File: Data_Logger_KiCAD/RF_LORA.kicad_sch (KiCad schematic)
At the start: 14 parts, among them U6 SX1262IMLTRT, U7 MASW-007221, Y1 Crystal_GND24

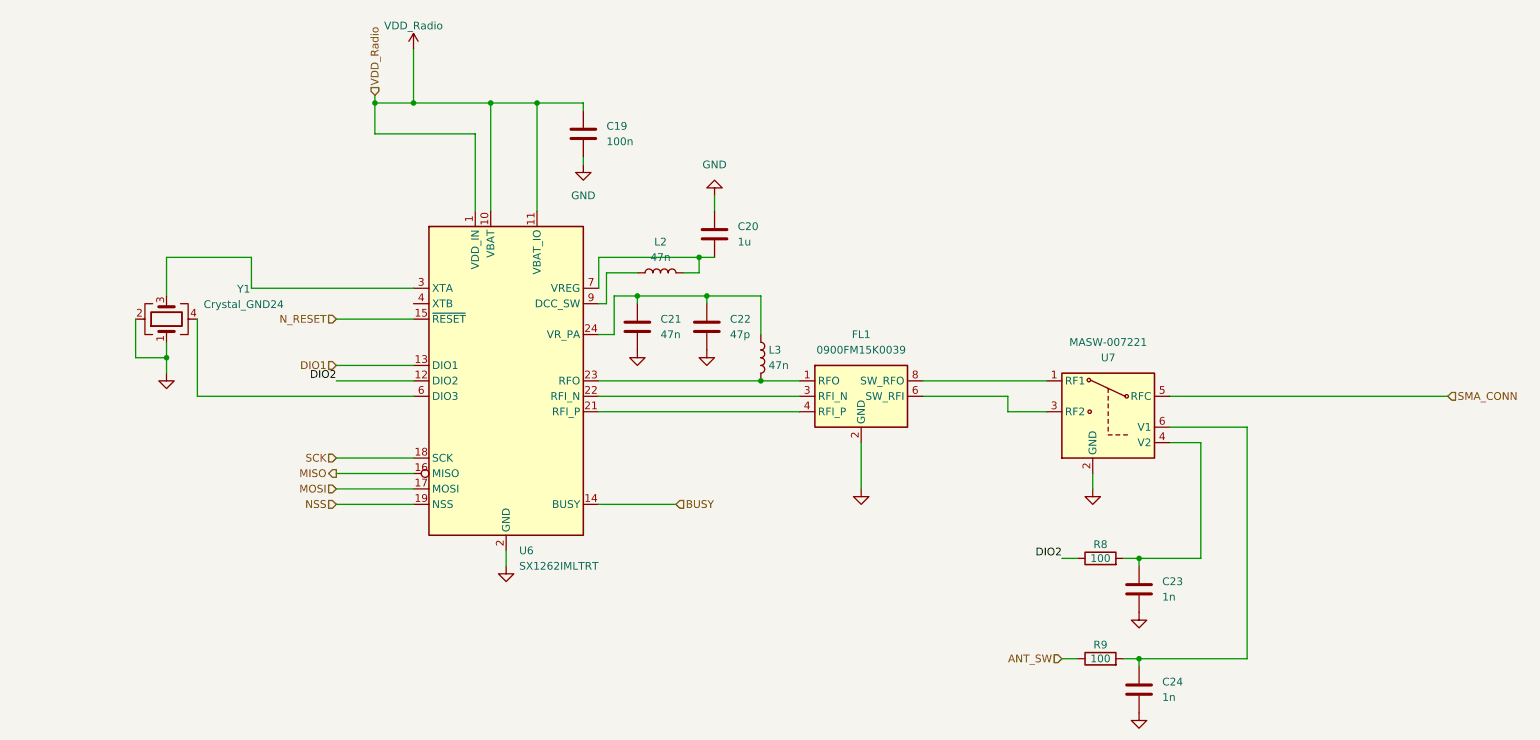
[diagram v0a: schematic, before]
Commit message: Added NT2016 TCXO Symbol and Footprint
Added NT2016 TCXO Symbol and Footprint
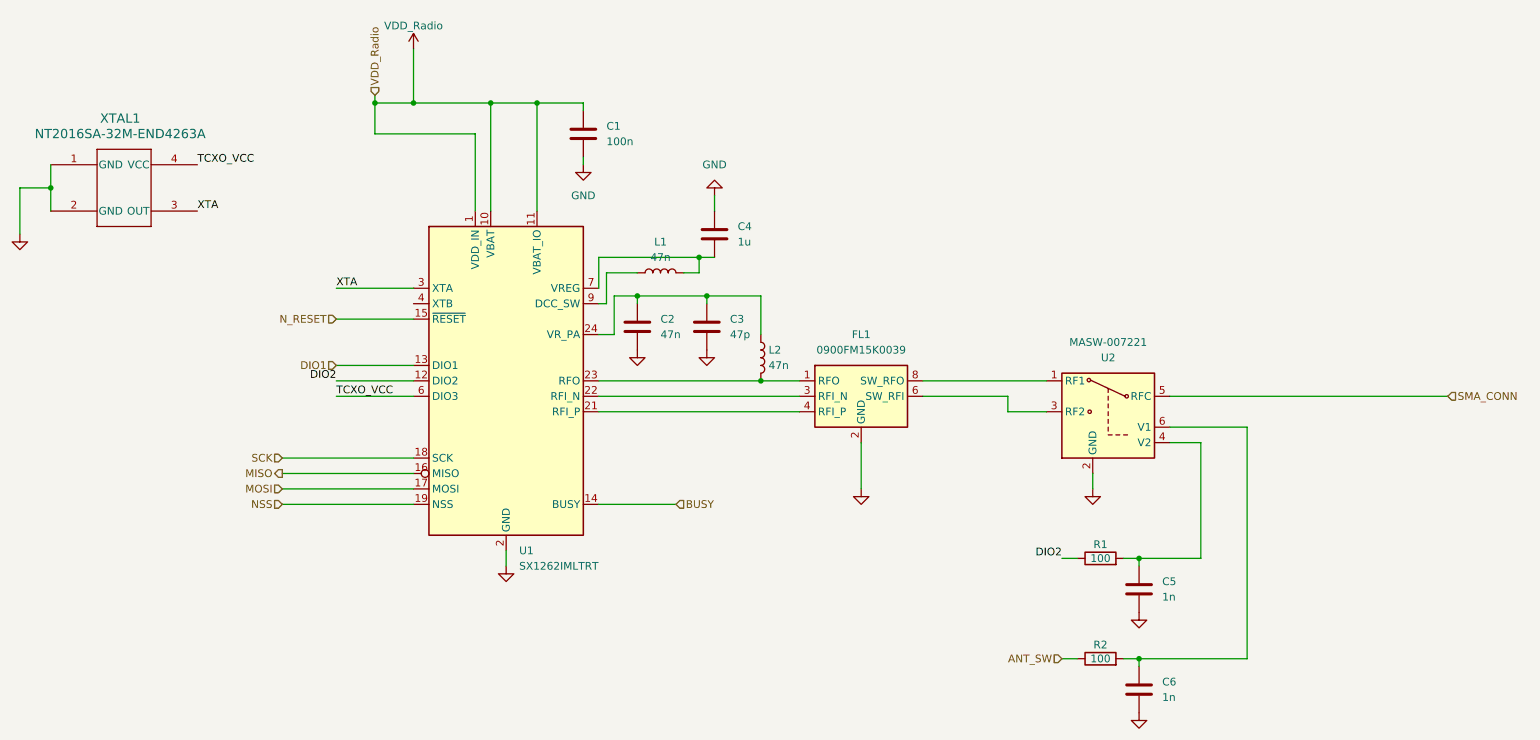
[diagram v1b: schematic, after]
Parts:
- removed Y1: Crystal_GND24, Crystal:Crystal_SMD_2520-4Pin_2.5x2.0mm, symbol Device:Crystal_GND24
- added XTAL1: NT2016SA-32M-END4263A, NT2016Footprints:NT2016SA-32M-END4263A_NDK, symbol NT2016_TCXO:NT2016SA-32M-END4263A
- renumbered C19 to C1, C21 to C2, C22 to C3, C20 to C4, C23 to C5, C24 to C6, L2 to L1, L3 to L2, R8 to R1, R9 to R2, U6 to U1, U7 to U2
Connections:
- net GND: now also XTAL1.1 (GND), XTAL1.2 (GND)
- net XTA: now reaches U1.3 (XTA)
- net XTA: now also XTAL1.3 (OUT)
- net TCXO_VCC: now reaches U1.6 (DIO3)
- net TCXO_VCC: now also XTAL1.4 (VCC)

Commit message: Magnetometer Footprint Added
Magnetometer Footprint Added
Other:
- company: (none) -> OSU ASDT
- title: (none) -> ASDT RF LoRa Schematic
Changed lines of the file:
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@@
 	(generator_version "9.0")
 	(paper "A4")
+	(title_block
+		(title "ASDT RF LoRa Schematic")
+		(rev "1.2 Last Rev:11/22/2025")
+		(company "OSU ASDT")
+		(comment 1 "Author: John Fletcher")
+	)
 	(junction
 		(at 96.52 38.1)

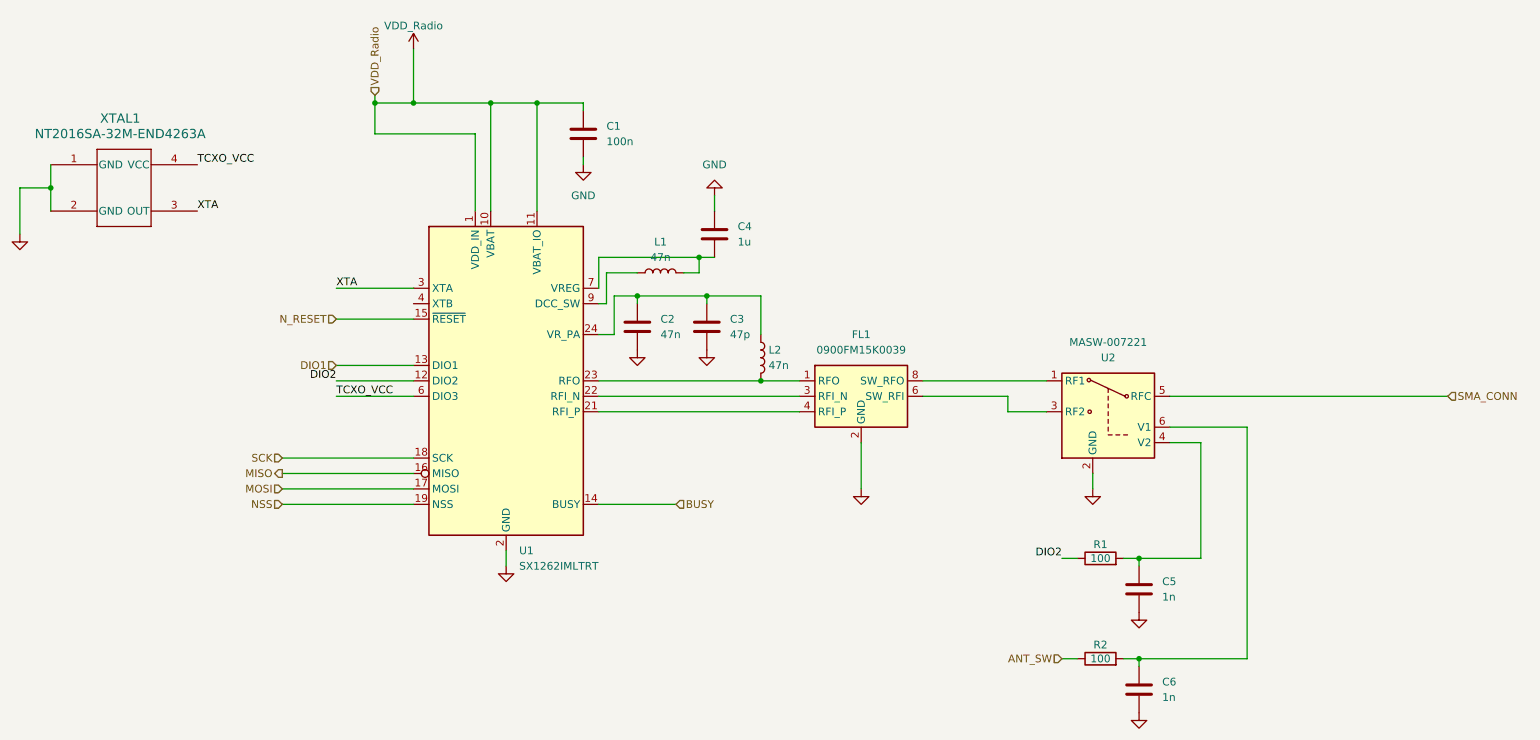
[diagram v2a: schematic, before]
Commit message: synced sheet pins in Data_Logger_Board_pro
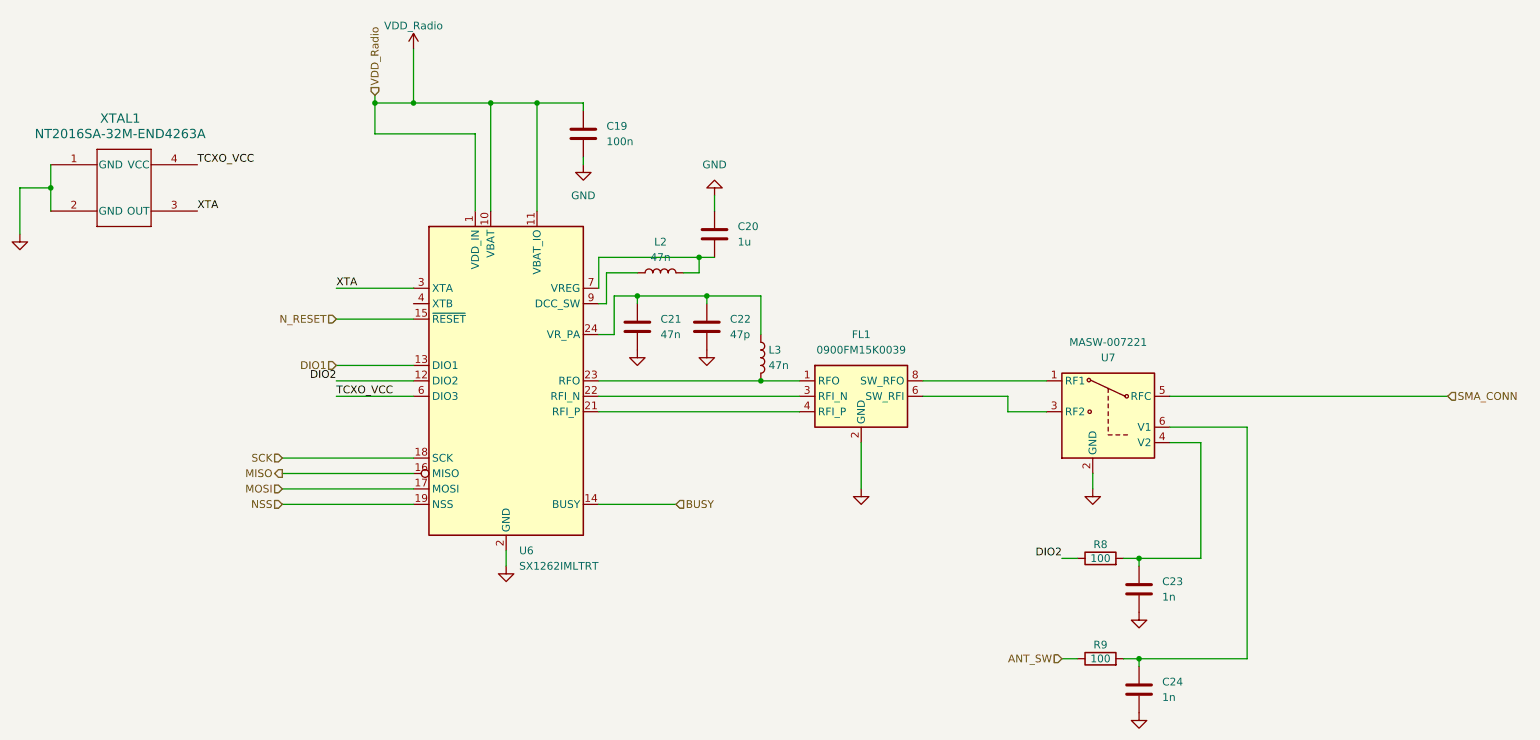
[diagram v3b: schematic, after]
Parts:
- renumbered C1 to C19, C4 to C20, C2 to C21, C3 to C22, C5 to C23, C6 to C24, L1 to L2, L2 to L3, R1 to R8, R2 to R9, U1 to U6, U2 to U7
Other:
- company: OSU ASDT -> (none)
- title: ASDT RF LoRa Schematic -> (none)
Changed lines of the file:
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@@
 	(generator_version "9.0")
 	(paper "A4")
-	(title_block
-		(title "ASDT RF LoRa Schematic")
-		(rev "1.2 Last Rev:11/22/2025")
-		(company "OSU ASDT")
-		(comment 1 "Author: John Fletcher")
-	)
 	(junction
 		(at 96.52 38.1)
@@
 		(dnp no)
 		(fields_autoplaced yes)
-		(property "Reference" "#PWR0105"
+		(property "Reference" "#PWR041"
 			(at 195.58 107.95 0)
 			(effects
@@
 		(on_board yes)
 		(dnp no)
-		(property "Reference" "R2"
+		(property "Reference" "R9"
 			(at 196.85 127.254 90)
 			(effects
@@
 		(dnp no)
 		(fields_autoplaced yes)
-		(property "Reference" "#PWR0108"
+		(property "Reference" "#PWR035"
 			(at 111.76 54.61 0)
 			(effects
@@
 		(on_board yes)
 		(dnp no)
-		(property "Reference" "U2"
+		(property "Reference" "U7"
 			(at 198.12 80.01 0)
 			(effects
@@
 		(dnp no)
 		(fields_autoplaced yes)
-		(property "Reference" "#PWR0103"
+		(property "Reference" "#PWR044"
 			(at 203.2 144.78 0)
 			(effects
@@
 		(dnp no)
 		(fields_autoplaced yes)
-		(property "Reference" "#PWR0101"
+		(property "Reference" "#PWR034"
 			(at 83.82 33.02 0)
 			(effects
@@
 		(dnp no)
 		(fields_autoplaced yes)
-		(property "Reference" "#PWR0106"
+		(property "Reference" "#PWR042"
 			(at 99.06 120.65 0)
 			(effects
@@
 		(dnp no)
 		(fields_autoplaced yes)
-		(property "Reference" "U1"
+		(property "Reference" "U6"
 			(at 101.2033 111.76 0)
 			(effects
@@
 		(dnp no)
 		(fields_autoplaced yes)
-		(property "Reference" "L1"
+		(property "Reference" "L2"
 			(at 124.46 60.96 90)
 			(effects
@@
 		(dnp no)
 		(fields_autoplaced yes)
-		(property "Reference" "L2"
+		(property "Reference" "L3"
 			(at 142.24 78.7399 0)
 			(effects
@@
 		(dnp no)
 		(fields_autoplaced yes)
-		(property "Reference" "#PWR0109"
+		(property "Reference" "#PWR036"
 			(at 133.35 46.99 0)
 			(effects
@@
 		(dnp no)
 		(fields_autoplaced yes)
-		(property "Reference" "C5"
+		(property "Reference" "C23"
 			(at 207.01 116.8399 0)
 			(effects
@@
 		(dnp no)
 		(fields_autoplaced yes)
-		(property "Reference" "#PWR0102"
+		(property "Reference" "#PWR040"
 			(at 157.48 107.95 0)
 			(effects
@@
 		(dnp no)
 		(fields_autoplaced yes)
-		(property "Reference" "#PWR0104"
+		(property "Reference" "#PWR043"
 			(at 203.2 128.27 0)
 			(effects
@@
 		(on_board yes)
 		(dnp no)
-		(property "Reference" "R1"
+		(property "Reference" "R8"
 			(at 196.85 110.744 90)
 			(effects
@@
 		(on_board yes)
 		(dnp no)
-		(property "Reference" "#PWR0110"
+		(property "Reference" "#PWR038"
 			(at 132.08 85.09 0)
 			(effects
@@
 		(on_board yes)
 		(dnp no)
-		(property "Reference" "C2"
+		(property "Reference" "C21"
 			(at 124.46 73.6599 0)
 			(effects
@@
 		(dnp no)
 		(fields_autoplaced yes)
-		(property "Reference" "C3"
+		(property "Reference" "C22"
 			(at 135.89 73.6599 0)
 			(effects
@@
 		(dnp no)
 		(fields_autoplaced yes)
-		(property "Reference" "XTAL1"
+		(property "Reference" "XTAL?"
 			(at 35.56 40.64 0)
 			(effects
@@
 				(path "/8ae4759a-151c-407c-bd9a-b8440b531f27"
 					(reference "XTAL1")
+					(unit 1)
+				)
+			)
+			(project "Data_Logger_Board"
+				(path "/db968e42-3ace-4cc9-9096-9d8f48135c40/795ab2be-9db7-4254-b05c-ac2b60177344/ddd17302-66df-4ba5-8c9c-bee0e050b0e0"
+					(reference "XTAL?")
 					(unit 1)
 				)
@@
 		(dnp no)
 		(fields_autoplaced yes)
-		(property "Reference" "#PWR0107"
+		(property "Reference" "#PWR037"
 			(at 120.65 85.09 0)
 			(effects
@@
 		(dnp no)
 		(fields_autoplaced yes)
-		(property "Reference" "C4"
+		(property "Reference" "C20"
 			(at 137.16 58.4199 0)
 			(effects
@@
 		(dnp no)
 		(fields_autoplaced yes)
-		(property "Reference" "C1"
+		(property "Reference" "C19"
 			(at 115.57 41.9099 0)
 			(effects
@@
 		(dnp no)
 		(fields_autoplaced yes)
-		(property "Reference" "#PWR01"
+		(property "Reference" "#PWR?"
 			(at 19.05 66.04 0)
 			(effects
@@
 				(path "/8ae4759a-151c-407c-bd9a-b8440b531f27"
 					(reference "#PWR01")
+					(unit 1)
+				)
+			)
+			(project "Data_Logger_Board"
+				(path "/db968e42-3ace-4cc9-9096-9d8f48135c40/795ab2be-9db7-4254-b05c-ac2b60177344/ddd17302-66df-4ba5-8c9c-bee0e050b0e0"
+					(reference "#PWR?")
 					(unit 1)
 				)
@@
 		(dnp no)
 		(fields_autoplaced yes)
-		(property "Reference" "C6"
+		(property "Reference" "C24"
 			(at 207.01 133.3499 0)
 			(effects

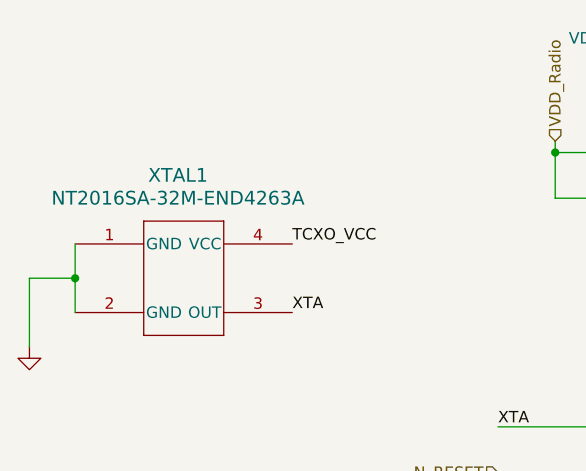
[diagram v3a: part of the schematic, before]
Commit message: rem old files and add LCSC #'s
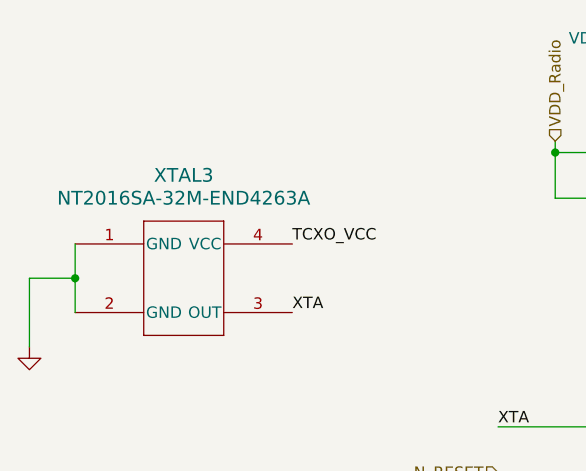
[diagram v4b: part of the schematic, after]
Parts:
- C19: LCSC (none) -> C1525
- C20: LCSC (none) -> C52923
- C21: footprint Capacitor_SMD:C_0402_1005Metric -> Capacitor_SMD:C_0603_1608Metric; LCSC (none) -> C1622
- C22: LCSC (none) -> C1567
- C23, C24: LCSC (none) -> C1523
- L2, L3: footprint Inductor_SMD:L_CommonModeChoke_Coilcraft_0603USB -> Inductor_SMD:L_0402_1005Metric; LCSC (none) -> C27151
- R8, R9: LCSC (none) -> C25076
- renumbered XTAL1 to XTAL3
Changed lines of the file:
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@@
+			)
+		)
+		(property "LCSC" "C25076"
+			(at 196.85 129.54 90)
+			(effects
+				(font
+					(size 1.27 1.27)
+				)
+				(hide yes)
 			)
 		)
@@
 			)
 		)
-		(property "Footprint" "Inductor_SMD:L_CommonModeChoke_Coilcraft_0603USB"
+		(property "Footprint" "Inductor_SMD:L_0402_1005Metric"
 			(at 124.46 66.04 0)
 			(effects
@@
 		(property "Description" "Inductor"
 			(at 124.46 66.04 0)
+			(effects
+				(font
+					(size 1.27 1.27)
+				)
+				(hide yes)
+			)
+		)
+		(property "LCSC" "C27151"
+			(at 124.46 66.04 90)
 			(effects
 				(font
@@
 			)
 		)
-		(property "Footprint" "Inductor_SMD:L_CommonModeChoke_Coilcraft_0603USB"
+		(property "Footprint" "Inductor_SMD:L_0402_1005Metric"
 			(at 140.97 80.01 0)
 			(effects
@@
 		)
 		(property "Description" "Inductor"
+			(at 140.97 80.01 0)
+			(effects
+				(font
+					(size 1.27 1.27)
+				)
+				(hide yes)
+			)
+		)
+		(property "LCSC" "C27151"
 			(at 140.97 80.01 0)
 			(effects
@@
 			)
 		)
+		(property "LCSC" "C1523"
+			(at 203.2 118.11 0)
+			(effects
+				(font
+					(size 1.27 1.27)
+				)
+				(hide yes)
+			)
+		)
 		(pin "2"
 		)
@@
 			)
 		)
+		(property "LCSC" "C25076"
+			(at 196.85 113.03 90)
+			(effects
+				(font
+					(size 1.27 1.27)
+				)
+				(hide yes)
+			)
+		)
 		(pin "2"
 		)
@@
 			)
 		)
-		(property "Footprint" "Capacitor_SMD:C_0402_1005Metric"
+		(property "Footprint" "Capacitor_SMD:C_0603_1608Metric"
 			(at 121.6152 78.74 0)
 			(effects
@@
 		)
 		(property "Description" "Unpolarized capacitor"
+			(at 120.65 74.93 0)
+			(effects
+				(font
+					(size 1.27 1.27)
+				)
+				(hide yes)
+			)
+		)
+		(property "LCSC" "C1622"
 			(at 120.65 74.93 0)
 			(effects
@@
 			)
 		)
+		(property "LCSC" "C1567"
+			(at 132.08 74.93 0)
+			(effects
+				(font
+					(size 1.27 1.27)
+				)
+				(hide yes)
+			)
+		)
 		(pin "2"
 		)
@@
 		(dnp no)
 		(fields_autoplaced yes)
-		(property "Reference" "XTAL?"
-			(at 35.56 40.64 0)
+		(property "Reference" "XTAL3"
+			(at 36.195 40.64 0)
 			(effects
 				(font
@@
 		)
 		(property "Value" "NT2016SA-32M-END4263A"
-			(at 35.56 43.18 0)
+			(at 36.195 43.18 0)
 			(effects
 				(font
@@
 			(project "Data_Logger_Board"
 				(path "/db968e42-3ace-4cc9-9096-9d8f48135c40/795ab2be-9db7-4254-b05c-ac2b60177344/ddd17302-66df-4ba5-8c9c-bee0e050b0e0"
-					(reference "XTAL?")
+					(reference "XTAL3")
 					(unit 1)
 				)
@@
 			)
 		)
+		(property "LCSC" "C52923"
+			(at 133.35 59.69 0)
+			(effects
+				(font
+					(size 1.27 1.27)
+				)
+				(hide yes)
+			)
+		)
 		(pin "2"
 		)
@@
 			)
 		)
+		(property "LCSC" "C1525"
+			(at 111.76 43.18 0)
+			(effects
+				(font
+					(size 1.27 1.27)
+				)
+				(hide yes)
+			)
+		)
 		(pin "2"
 		)
@@
 			(at 203.2 134.62 0)
 			(effects
+				(font
+					(size 1.27 1.27)
+				)
+				(hide yes)
+			)
+		)
+		(property "LCSC" "C1523"
+			(at 203.2 134.62 0)
+			(effects

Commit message: fix footprint errors
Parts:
- XTAL3: footprint NT2016Footprints:NT2016SA-32M-END4263A_NDK -> custom:NT2016SA-32M-END4263A_NDK
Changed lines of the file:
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@@
 			)
 		)
-		(property "Footprint" "NT2016Footprints:NT2016SA-32M-END4263A_NDK"
+		(property "Footprint" "custom:NT2016SA-32M-END4263A_NDK"
 			(at 15.24 50.8 0)
 			(effects
